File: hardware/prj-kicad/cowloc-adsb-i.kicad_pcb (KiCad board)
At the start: 2 copper layers, 15 parts, among them U1 NSVG3117

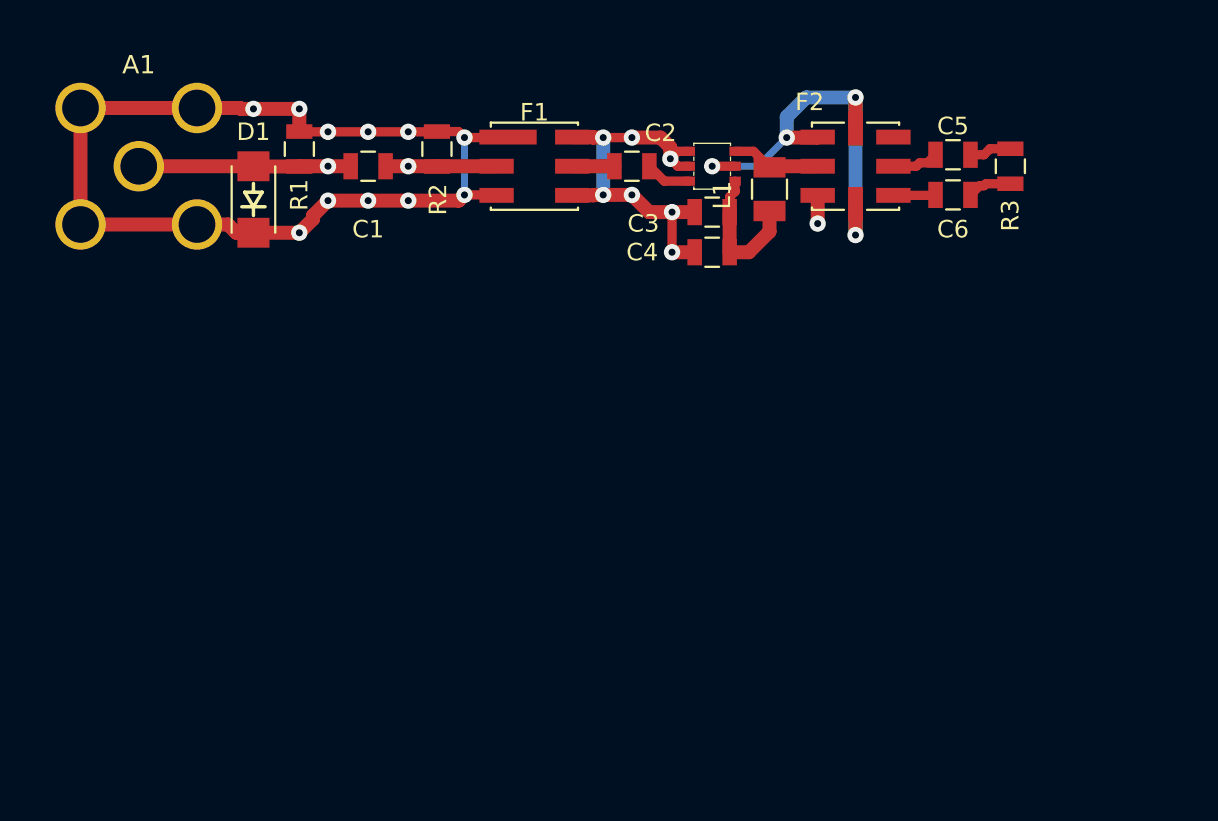
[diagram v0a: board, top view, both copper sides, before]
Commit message: = ADD: Insert a first signal detector based on AD8313
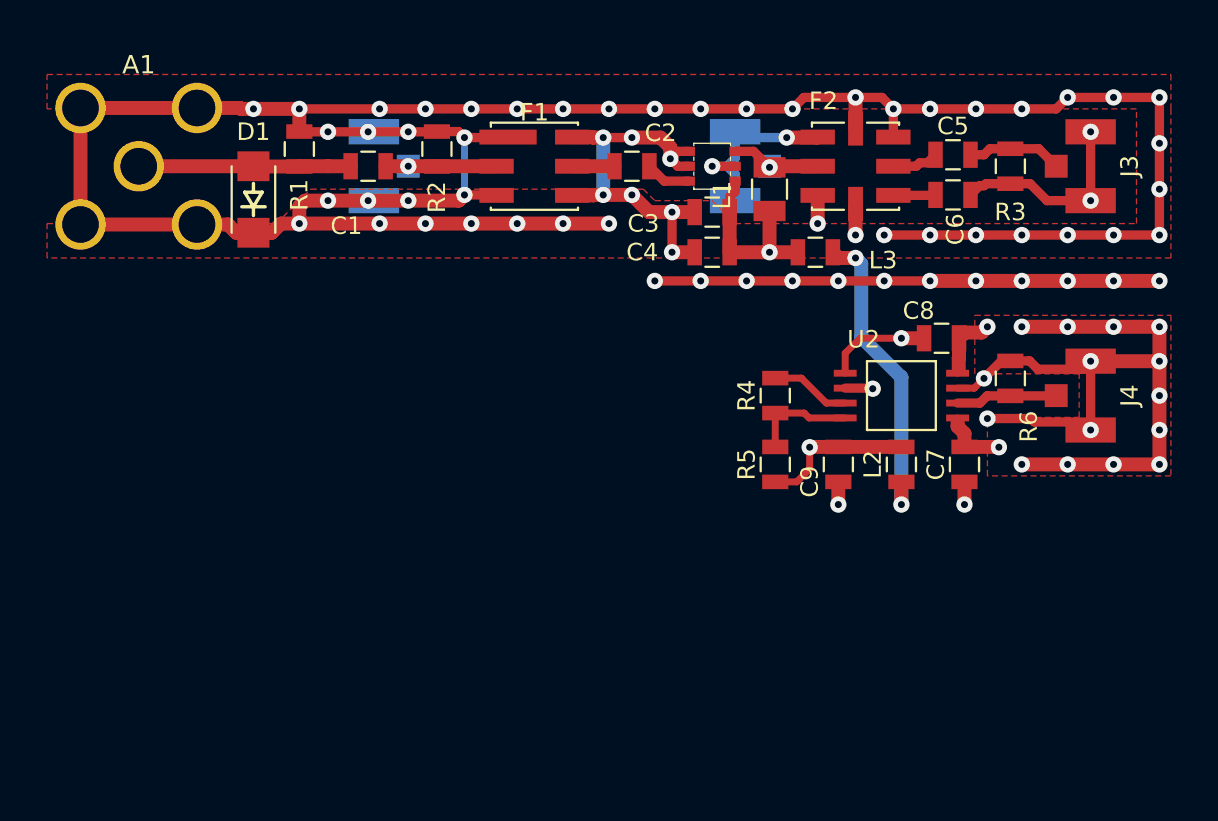
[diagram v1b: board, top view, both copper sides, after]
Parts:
- added C7: 10nF, cowloc-adsb-i:SMD0603, F.Cu at (156.0, 118.0)
- added C8: 10nF, cowloc-adsb-i:SMD0603, F.Cu at (155.0, 112.5)
- added C9: 100nF, cowloc-adsb-i:SMD0603, F.Cu at (150.5, 118.0)
- added J1: ~, cowloc-adsb-i:CONN_UFL-R-SMT-1, B.Cu at (130.2, 105.0)
- added J2: ~, cowloc-adsb-i:CONN_UFL-R-SMT-1, B.Cu at (146.0, 105.0)
- added J3: ~, cowloc-adsb-i:CONN_UFL-R-SMT-1, F.Cu at (161.5, 105.0)
- added J4: ~, cowloc-adsb-i:CONN_UFL-R-SMT-1, F.Cu at (161.5, 115.0)
- added L2: FB100, cowloc-adsb-i:SMD0603, F.Cu at (153.2, 118.0)
- added L3: FB100, cowloc-adsb-i:SMD0603, F.Cu at (149.5, 108.8)
- added R4: 4,7k, cowloc-adsb-i:SMD0603, F.Cu at (147.8, 115.0)
- added R5: n/e, cowloc-adsb-i:SMD0603, F.Cu at (147.8, 118.0)
- added R6: n/e, cowloc-adsb-i:SMD0603, F.Cu at (158.0, 114.2)
- added U2: AD8313, cowloc-adsb-i:MSOP-8, F.Cu at (153.2, 115.0)
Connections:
- net Net-(C1-Pad2) renamed TPRF1
- net Net-(F2-Pad2) renamed TPRF2
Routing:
- net GND: track 84.5 -> 199.3 mm, vias 23 -> 71
- net Net-(U2-INLO): track 0.00 -> 35.6 mm, vias 0 -> 15
- net /VDET_1: track 0.00 -> 27.5 mm, vias 0 -> 3
- net +5V: track 0.00 -> 13.7 mm, vias 0 -> 2
- net Net-(C6-Pad2): track 1.94 -> 8.75 mm, vias 0 -> 2
- net DET1: track 0.00 -> 4.61 mm
- net Net-(U2-INHI): track 0.00 -> 4.43 mm
- net Net-(U2-VSET): track 0.00 -> 3.50 mm
- net Net-(C5-Pad2): track 1.85 -> 4.16 mm
- net +VLNA: track 6.21 -> 7.97 mm, vias 0 -> 1
- net TPRF2: vias 0 -> 1
- net Net-(D1-K): vias 1 -> 0
- added copper zone on In2.Cu, net +5V
- added copper zone on In2.Cu, net +VLNA
- added copper zone on In2.Cu, net /VDET_1
- added copper zone on F.Cu, net GND
- added copper zone on In1.Cu, net GND
- added copper zone on F.Cu, net Net-(U2-INLO)
- added copper zone on In1.Cu, net Net-(U2-INLO)
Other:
- copper layers 2 -> 4

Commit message: = ADD: Insert an alternate signal detector (AD993x) and a comparator on output
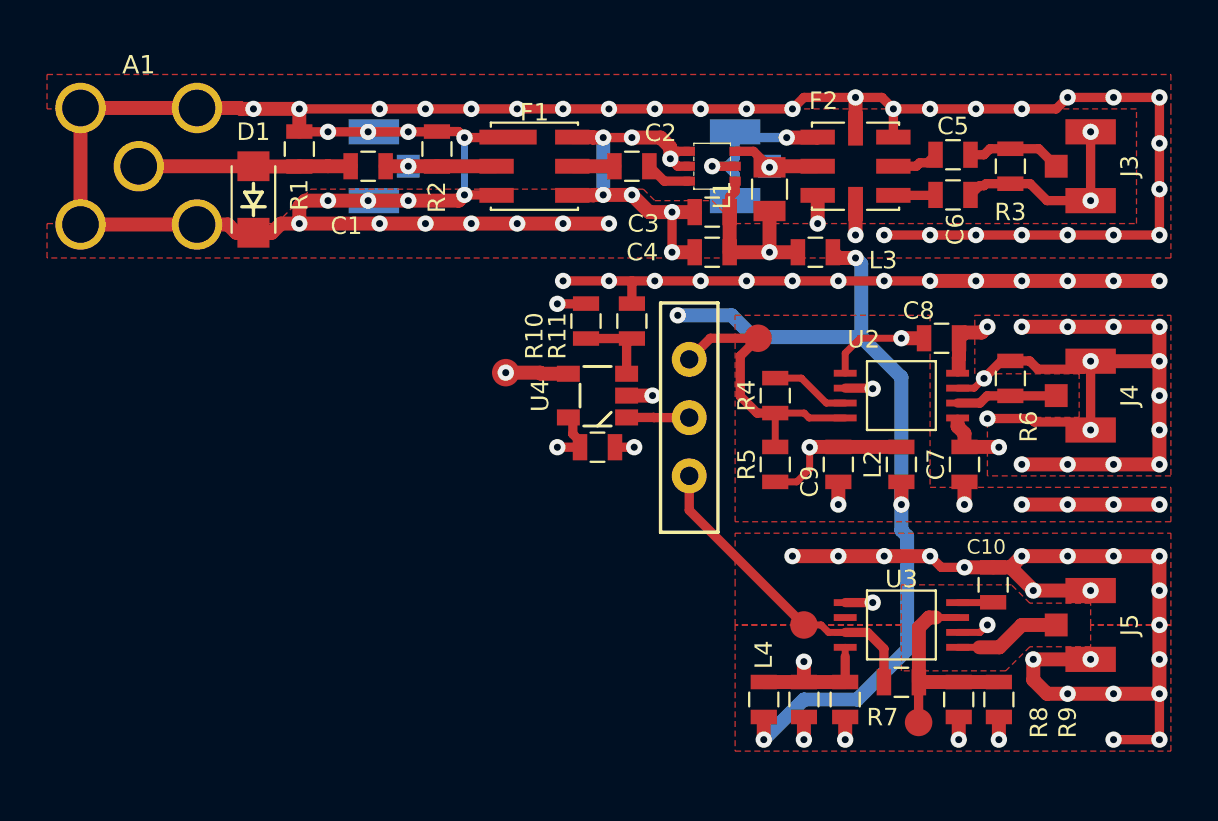
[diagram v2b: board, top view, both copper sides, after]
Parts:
- added C10: C, cowloc-adsb-i:SMD0603, F.Cu at (157.2, 123.2)
- added C11: 10nF, cowloc-adsb-i:SMD0603, F.Cu at (150.8, 128.2)
- added C12: 100nF, cowloc-adsb-i:SMD0603, F.Cu at (149.0, 128.2)
- added C13: 100nF, cowloc-adsb-i:SMD0603, F.Cu at (140.0, 117.2)
- added J5: ~, cowloc-adsb-i:CONN_UFL-R-SMT-1, F.Cu at (161.5, 125.0)
- added L4: FB100, cowloc-adsb-i:SMD0603, F.Cu at (147.2, 128.2)
- added P1: CONN_1, cowloc-adsb-i:TP_SMD, F.Cu at (136.0, 114.0)
- added R10: R, cowloc-adsb-i:SMD0603, F.Cu at (139.5, 111.8)
- added R11: R, cowloc-adsb-i:SMD0603, F.Cu at (141.5, 111.8)
- added R7: R, cowloc-adsb-i:SMD0603, F.Cu at (153.2, 127.5)
- added R8: R, cowloc-adsb-i:SMD0603, F.Cu at (155.8, 128.2)
- added R9: R, cowloc-adsb-i:SMD0603, F.Cu at (157.5, 128.2)
- added SW1: SWITCH_SLIDE, cowloc-adsb-i:SW_450301014042, F.Cu at (144.0, 116.0)
- added TP1: CONN_1, cowloc-adsb-i:TP_SMD, F.Cu at (147.0, 112.5)
- added TP2: CONN_1, cowloc-adsb-i:TP_SMD, F.Cu at (149.0, 125.0)
- added TP3: CONN_1, cowloc-adsb-i:TP_SMD, F.Cu at (154.0, 129.2)
- added U3: AD993x, cowloc-adsb-i:MSOP-8, F.Cu at (153.2, 125.0)
- added U4: HT8051, cowloc-adsb-i:SOT23-5, F.Cu at (140.0, 115.0)
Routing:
- net GND: track 199.3 -> 285.5 mm, vias 71 -> 104
- net +5V: track 13.7 -> 41.1 mm, vias 2 -> 6
- net +VDET2: track 0.00 -> 21.8 mm, vias 0 -> 3
- net DET2: track 0.00 -> 14.0 mm
- net Net-(U3-(SET)): track 0.00 -> 9.50 mm
- net DET1: track 4.61 -> 12.7 mm
- net Net-(U3-RF_IN): track 0.00 -> 4.70 mm
- net Net-(U4--): track 0.00 -> 3.63 mm
- net Net-(P1-Pad1): track 0.00 -> 2.75 mm, vias 0 -> 1
- net Net-(U4-+): track 0.00 -> 2.74 mm
- net Net-(U3-CLPF): track 0.00 -> 1.56 mm
- added copper zone on In2.Cu, net +VDET2

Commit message: = ADD: Insert an hard-wired signal decoder (beta!!)
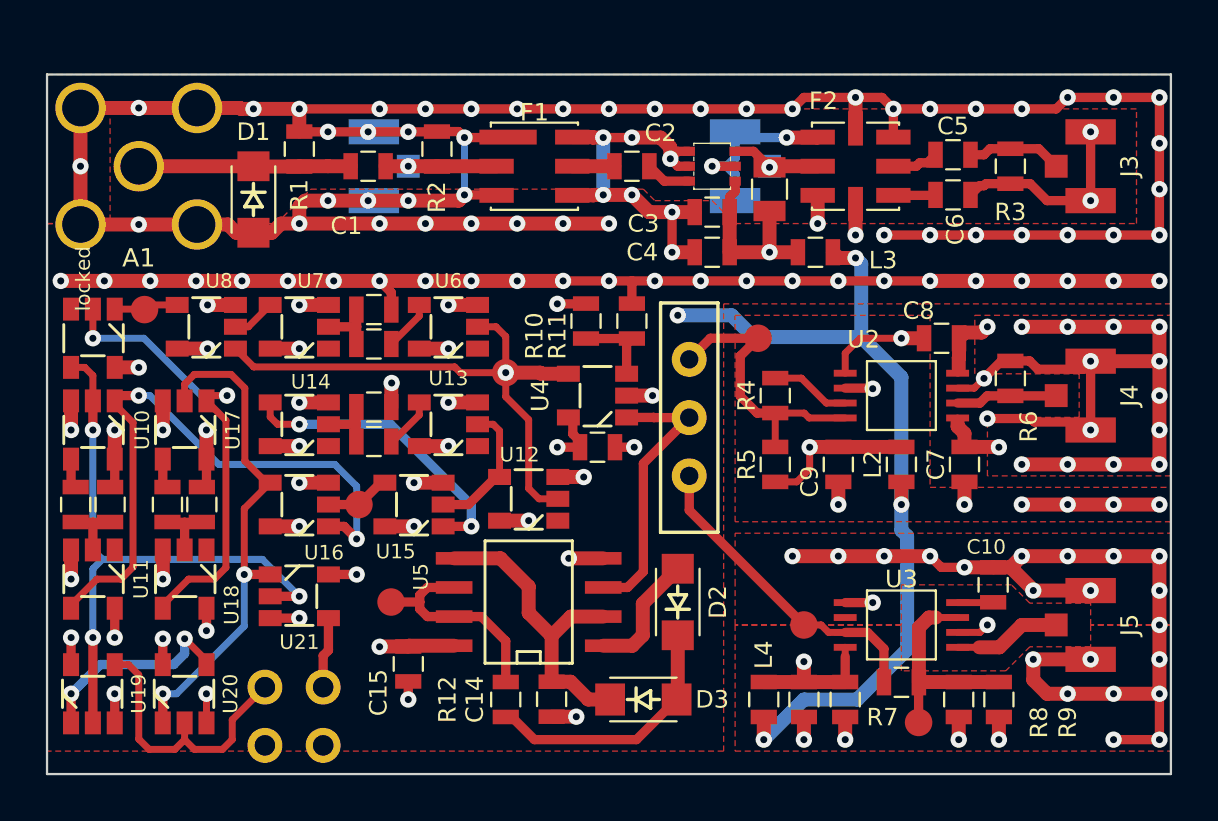
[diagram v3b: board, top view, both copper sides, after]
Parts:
- added C14: 100nF, cowloc-adsb-i:SMD0603, F.Cu at (138.0, 128.2)
- added C15: 100nF, cowloc-adsb-i:SMD0603, F.Cu at (131.8, 126.7)
- added C16: C, cowloc-adsb-i:SMD0603, F.Cu at (130.2, 111.2)
- added C17: C, cowloc-adsb-i:SMD0603, F.Cu at (117.2, 119.8)
- added C18: C, cowloc-adsb-i:SMD0603, F.Cu at (130.2, 115.5)
- added C19: C, cowloc-adsb-i:SMD0603, F.Cu at (121.2, 119.8)
- added D2: D, cowloc-adsb-i:SOD-123, F.Cu at (143.5, 124.0)
- added D3: D, cowloc-adsb-i:SOD-123, F.Cu at (142.0, 128.2)
- added P1: CONN_1, cowloc-adsb-i:TP_PIN, F.Cu at (125.5, 130.2)
- added P2: CONN_1, cowloc-adsb-i:TP_PIN, F.Cu at (128.0, 130.2)
- added P3: CONN_1, cowloc-adsb-i:TP_PIN, F.Cu at (125.5, 127.7)
- added P4: CONN_1, cowloc-adsb-i:TP_PIN, F.Cu at (128.0, 127.7)
- added R12: R, cowloc-adsb-i:SMD0603, F.Cu at (136.0, 128.2)
- added R13: R, cowloc-adsb-i:SMD0603, F.Cu at (130.2, 112.8)
- added R14: R, cowloc-adsb-i:SMD0603, F.Cu at (118.8, 119.8)
- added R15: R, cowloc-adsb-i:SMD0603, F.Cu at (130.2, 117.0)
- added R16: R, cowloc-adsb-i:SMD0603, F.Cu at (122.8, 119.8)
- added TP5: CONN_1, cowloc-adsb-i:TP_SMD, F.Cu at (131.0, 124.0)
- added TP6: CONN_1, cowloc-adsb-i:TP_SMD, F.Cu at (120.2, 111.2)
- added TP7: CONN_1, cowloc-adsb-i:TP_SMD, F.Cu at (129.6, 119.8)
- added U10: SN74LVC1G02, cowloc-adsb-i:SOT23-5, F.Cu at (118.0, 116.5)
- added U11: SN74LVC1G14, cowloc-adsb-i:SOT23-5, F.Cu at (118.0, 123.0)
- added U12: SN74LVC1G14, cowloc-adsb-i:SOT23-5, F.Cu at (137.0, 119.5)
- added U13: SN74LVC1G17, cowloc-adsb-i:SOT23-5, F.Cu at (133.5, 116.2)
- added U14: SN74LVC1G14, cowloc-adsb-i:SOT23-5, F.Cu at (127.0, 116.2)
- added U15: SN74LVC1G08, cowloc-adsb-i:SOT23-5, F.Cu at (132.0, 119.8)
- added U16: SN74LVC1G08, cowloc-adsb-i:SOT23-5, F.Cu at (127.0, 119.8)
- added U17: SN74LVC1G02, cowloc-adsb-i:SOT23-5, F.Cu at (122.0, 116.5)
- added U18: SN74LVC1G14, cowloc-adsb-i:SOT23-5, F.Cu at (122.0, 123.0)
- added U19: SN74LVC1G02, cowloc-adsb-i:SOT23-5, F.Cu at (118.0, 128.0)
- added U20: SN74LVC1G02, cowloc-adsb-i:SOT23-5, F.Cu at (122.0, 128.0)
- added U21: SN74LVC1G02, cowloc-adsb-i:SOT23-5, F.Cu at (127.0, 123.8)
- added U5: TLV9062, cowloc-adsb-i:SOIC-8, F.Cu at (137.0, 124.0)
- added U6: SN74LVC1G17, cowloc-adsb-i:SOT23-5, F.Cu at (133.5, 112.0)
- added U7: SN74LVC1G14, cowloc-adsb-i:SOT23-5, F.Cu at (127.0, 112.0)
- added U8: SN74LVC1G08, cowloc-adsb-i:SOT23-5, F.Cu at (122.9, 112.0)
- added locked: SN74LVC1G08, cowloc-adsb-i:SOT23-5, F.Cu at (118.0, 112.5)
- renumbered P1 to TP4
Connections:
- net Net-(P1-Pad1) renamed SIG
- net Net-(U4-+) renamed DET
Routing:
- net GND: track 285.5 -> 363.4 mm, vias 104 -> 137
- net +5V: track 41.1 -> 97.8 mm, vias 6 -> 23
- net SIG_RISE: track 0.00 -> 27.1 mm, vias 0 -> 2
- net SIG_BIT1: track 0.00 -> 27.1 mm, vias 0 -> 3
- net SIG_BIT0: track 0.00 -> 22.3 mm, vias 0 -> 2
- net SIG: track 2.75 -> 24.9 mm
- net SIG_FALL: track 0.00 -> 20.3 mm, vias 0 -> 2
- net Net-(D3-K): track 0.00 -> 13.8 mm
- net Net-(U14-Y): track 0.00 -> 13.2 mm, vias 0 -> 2
- net /SIG_OUT: track 0.00 -> 12.4 mm
- net Net-(D2-K): track 0.00 -> 11.4 mm
- net Net-(U5B--): track 0.00 -> 9.61 mm
- net DET: track 2.74 -> 12.3 mm
- net Net-(U19-B): track 0.00 -> 9.13 mm, vias 0 -> 2
- net Net-(U12-Y): track 0.00 -> 6.05 mm
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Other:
- board outline added: 49 x 30.5 mm
